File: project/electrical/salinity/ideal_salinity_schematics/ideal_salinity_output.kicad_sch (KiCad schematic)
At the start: 13 parts, among them U1 MCP6L01, U2 MCP6L01, U3 MCP6L01

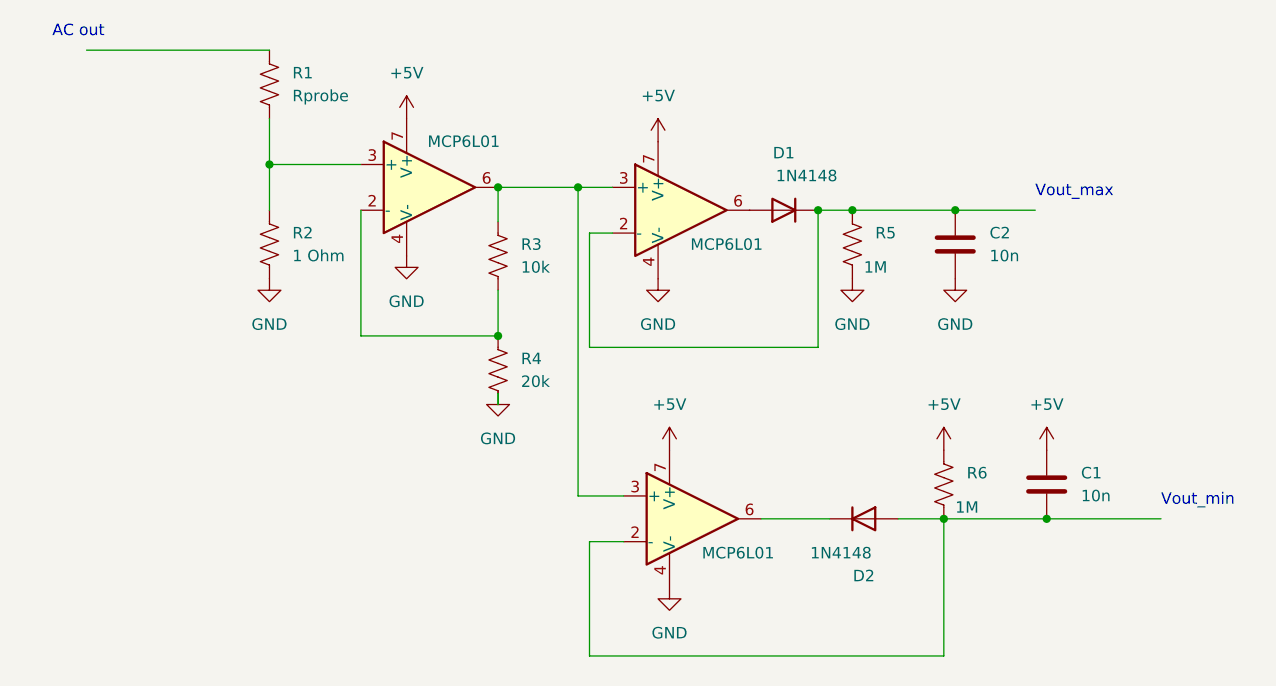
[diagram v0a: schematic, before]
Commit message: updated ideal salinity schematics
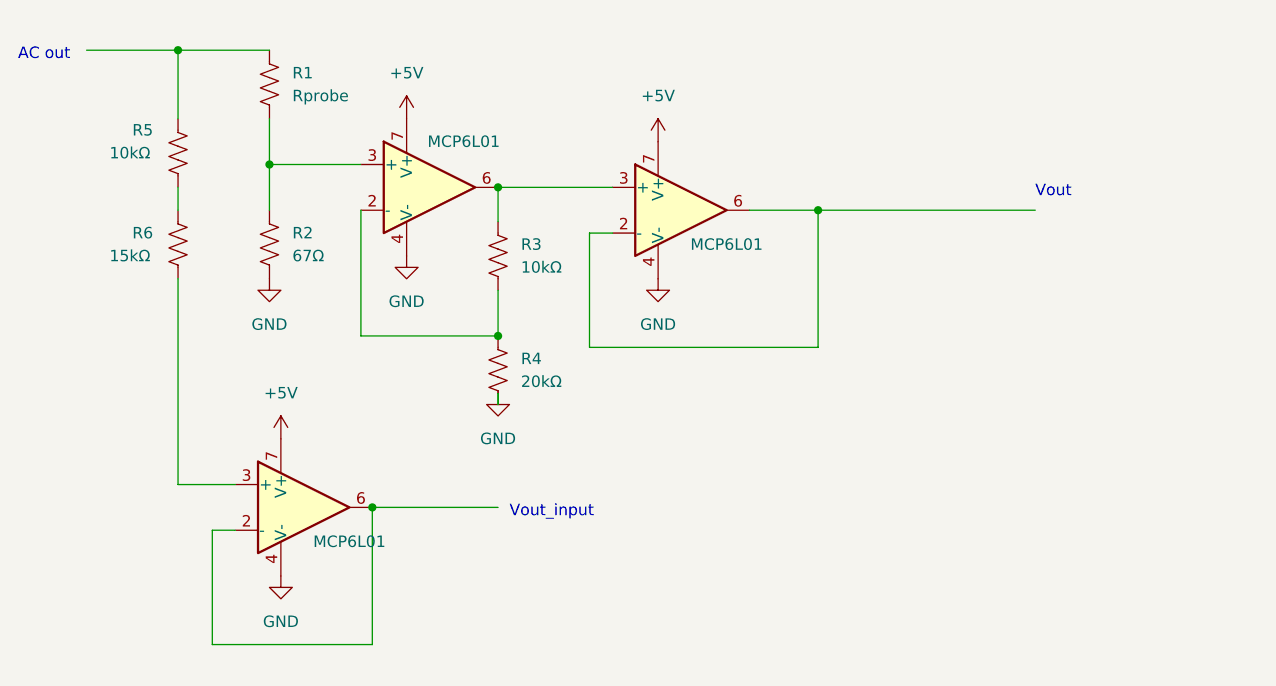
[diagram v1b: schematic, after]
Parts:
- removed C1, C2: 10n, symbol Device:C
- removed D1, D2: 1N4148, symbol Device:D
- R2: value 1 Ohm -> 67Ω
- R3: value 10k -> 10kΩ
- R4: value 20k -> 20kΩ
- R5: value 1M -> 10kΩ
- R6: value 1M -> 15kΩ
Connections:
- net +5V: no longer R6.1
- net GND: no longer R5.2
- net at U2.2 (-): now also U2.6; no longer R5.1
- net at R3.1, U1.6, U2.3 (+): no longer U3.3 (+)
- net at U3.2 (-): now also U3.6; no longer R6.2
- net at R1.1: now also R5.1
- new net: R6.2, U3.3 (+)
- new net: R5.2, R6.1
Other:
- note added: "Vout"
- note added: "Vout_input"
- note removed: "Vout_max"
- note removed: "Vout_min"

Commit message: schematics
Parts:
- R2: value 67Ω -> 68Ω
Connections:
- net GND: now also R6.2
- net at U3.3 (+): now also R5.2, R6.1; no longer R6.2
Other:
- moved on the sheet: R5, R6
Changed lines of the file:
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@@
   (junction (at 73.66 121.92) (diameter 0) (color 0 0 0 0)
   )
+  (junction (at 50.8 71.12) (diameter 0) (color 0 0 0 0)
+  )
   (junction (at 87.63 102.87) (diameter 0) (color 0 0 0 0)
   )
@@
   (junction (at 123.19 88.9) (diameter 0) (color 0 0 0 0)
   )
-  (junction (at 52.07 71.12) (diameter 0) (color 0 0 0 0)
-  )
   (junction (at 87.63 86.36) (diameter 0) (color 0 0 0 0)
   )
+  (junction (at 50.8 119.38) (diameter 0) (color 0 0 0 0)
+  )
   (wire (pts (xy 62.23 78.74) (xy 62.23 83.82))
     (stroke (width 0) (type default))
   )
-  (wire (pts (xy 52.07 119.38) (xy 58.42 119.38))
+  (wire (pts (xy 50.8 129.54) (xy 50.8 133.35))
     (stroke (width 0) (type default))
   )
@@
     (stroke (width 0) (type default))
   )
-  (wire (pts (xy 52.07 71.12) (xy 62.23 71.12))
+  (wire (pts (xy 50.8 71.12) (xy 62.23 71.12))
     (stroke (width 0) (type default))
   )
@@
     (stroke (width 0) (type default))
   )
-  (wire (pts (xy 52.07 71.12) (xy 52.07 78.74))
+  (wire (pts (xy 50.8 119.38) (xy 50.8 115.57))
+    (stroke (width 0) (type default))
+  )
+  (wire (pts (xy 50.8 119.38) (xy 58.42 119.38))
+    (stroke (width 0) (type default))
+  )
+  (wire (pts (xy 50.8 71.12) (xy 50.8 107.95))
     (stroke (width 0) (type default))
   )
@@
     (stroke (width 0) (type default))
   )
-  (wire (pts (xy 52.07 88.9) (xy 52.07 86.36))
+  (wire (pts (xy 50.8 121.92) (xy 50.8 119.38))
     (stroke (width 0) (type default))
   )
@@
     (stroke (width 0) (type default))
   )
-  (wire (pts (xy 41.91 71.12) (xy 52.07 71.12))
-    (stroke (width 0) (type default))
-  )
-  (wire (pts (xy 52.07 96.52) (xy 52.07 119.38))
+  (wire (pts (xy 41.91 71.12) (xy 50.8 71.12))
     (stroke (width 0) (type default))
   )
@@
     )
   )
+  (symbol (lib_id "power:GND") (at 50.8 133.35 0) (unit 1)
+    (in_bom yes) (on_board yes) (dnp no) (fields_autoplaced)
+    (property "Reference" "#PWR06" (at 50.8 139.7 0)
+      (effects (font (size 1.27 1.27)) hide)
+    )
+    (property "Value" "GND" (at 50.8 138.43 0)
+      (effects (font (size 1.27 1.27)))
+    )
+    (property "Footprint" "" (at 50.8 133.35 0)
+      (effects (font (size 1.27 1.27)) hide)
+    )
+    (property "Datasheet" "" (at 50.8 133.35 0)
+      (effects (font (size 1.27 1.27)) hide)
+    )
+    (pin "1")
+    (instances
+      (project "ideal_salinity_output"
+        (path "/c65a21d9-20a5-4e14-a1e3-194a093334b0"
+          (reference "#PWR06") (unit 1)
+        )
+      )
+    )
+  )
   (symbol (lib_id "power:+5V") (at 105.41 81.28 0) (unit 1)
     (in_bom yes) (on_board yes) (dnp no) (fields_autoplaced)
@@
     )
   )
-  (symbol (lib_id "Device:R_US") (at 52.07 82.55 0) (unit 1)
-    (in_bom yes) (on_board yes) (dnp no)
-    (property "Reference" "R5" (at 46.99 80.01 0)
-      (effects (font (size 1.27 1.27)) (justify left))
-    )
-    (property "Value" "10kΩ" (at 44.45 82.55 0)
-      (effects (font (size 1.27 1.27)) (justify left))
-    )
-    (property "Footprint" "" (at 53.086 82.804 90)
-      (effects (font (size 1.27 1.27)) hide)
-    )
-    (property "Datasheet" "~" (at 52.07 82.55 0)
+  (symbol (lib_id "Device:R_US") (at 50.8 111.76 0) (unit 1)
+    (in_bom yes) (on_board yes) (dnp no)
+    (property "Reference" "R5" (at 45.72 109.22 0)
+      (effects (font (size 1.27 1.27)) (justify left))
+    )
+    (property "Value" "10kΩ" (at 43.18 111.76 0)
+      (effects (font (size 1.27 1.27)) (justify left))
+    )
+    (property "Footprint" "" (at 51.816 112.014 90)
+      (effects (font (size 1.27 1.27)) hide)
+    )
+    (property "Datasheet" "~" (at 50.8 111.76 0)
       (effects (font (size 1.27 1.27)) hide)
     )
@@
     )
   )
-  (symbol (lib_id "Device:R_US") (at 52.07 92.71 0) (unit 1)
-    (in_bom yes) (on_board yes) (dnp no)
-    (property "Reference" "R6" (at 46.99 91.44 0)
-      (effects (font (size 1.27 1.27)) (justify left))
-    )
-    (property "Value" "15kΩ" (at 44.45 93.98 0)
-      (effects (font (size 1.27 1.27)) (justify left))
-    )
-    (property "Footprint" "" (at 53.086 92.964 90)
-      (effects (font (size 1.27 1.27)) hide)
-    )
-    (property "Datasheet" "~" (at 52.07 92.71 0)
+  (symbol (lib_id "Device:R_US") (at 50.8 125.73 0) (unit 1)
+    (in_bom yes) (on_board yes) (dnp no)
+    (property "Reference" "R6" (at 45.72 124.46 0)
+      (effects (font (size 1.27 1.27)) (justify left))
+    )
+    (property "Value" "15kΩ" (at 43.18 127 0)
+      (effects (font (size 1.27 1.27)) (justify left))
+    )
+    (property "Footprint" "" (at 51.816 125.984 90)
+      (effects (font (size 1.27 1.27)) hide)
+    )
+    (property "Datasheet" "~" (at 50.8 125.73 0)
       (effects (font (size 1.27 1.27)) hide)
     )
@@
   )
   (symbol (lib_id "Device:R_US") (at 62.23 74.93 0) (unit 1)
-    (in_bom yes) (on_board yes) (dnp no) (fields_autoplaced)
+    (in_bom yes) (on_board yes) (dnp no)
     (property "Reference" "R1" (at 64.77 73.66 0)
-      (effects (font (size 1.27 1.27)) (justify left))
-    )
-    (property "Value" "Rprobe" (at 64.77 76.2 0)
+      (effects (font (size 1.27 1.27)) (justify left) hide)
+    )
+    (property "Value" "Rprobe" (at 64.77 74.93 0)
       (effects (font (size 1.27 1.27)) (justify left))
     )
@@
       (effects (font (size 1.27 1.27)) (justify left))
     )
-    (property "Value" "67Ω" (at 64.77 93.98 0)
-      (effects (font (size 1.27 1.27)) (justify left))
-    )
+    (property "Value" "68Ω" (at 64.77 93.98 0)
+      (effects (font (size 1.27 1.27)) (justify left))
+    )
